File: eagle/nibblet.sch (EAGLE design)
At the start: 35 parts, among them IC1 MEGA8-AI

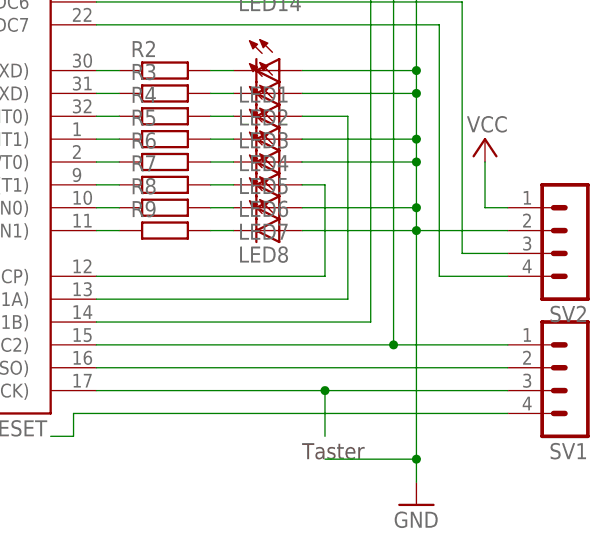
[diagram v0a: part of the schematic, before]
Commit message: consistent led order
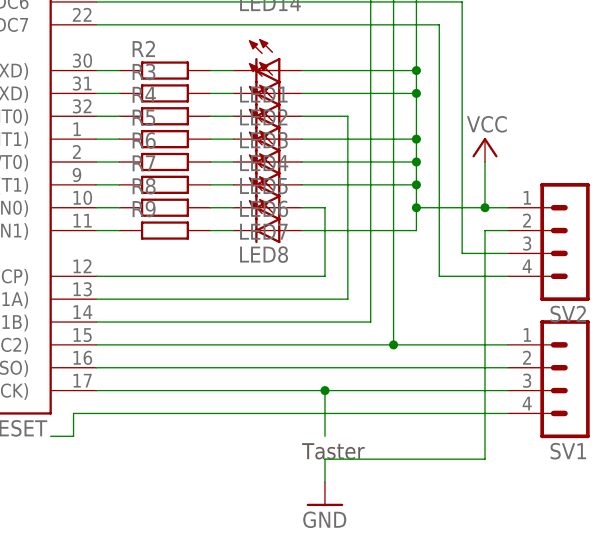
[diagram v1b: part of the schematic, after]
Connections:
- net GND: no longer LED1.A, LED11.A, LED12.A, LED13.A, LED2.A, LED4.A, LED5.A, LED7.A, LED8.A, LED9.A
- net N$23: now also LED7.A; no longer LED6.A
- net VCC: now also LED1.A, LED11.A, LED12.A, LED13.A, LED2.A, LED4.A, LED5.A, LED6.A, LED8.A, LED9.A
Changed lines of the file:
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@@
 <instance part="C2" gate="G$1" x="15.24" y="88.9" rot="R180"/>
 <instance part="P+2" gate="VCC" x="10.16" y="63.5"/>
-<instance part="GND2" gate="1" x="106.68" y="25.4"/>
+<instance part="GND2" gate="1" x="96.52" y="25.4"/>
 <instance part="PAD1" gate="G$1" x="5.08" y="86.36"/>
 <instance part="SV1" gate="1" x="124.46" y="38.1" rot="R180"/>
@@
 <pinref part="P+3" gate="VCC" pin="VCC"/>
 <pinref part="SV2" gate="1" pin="1"/>
+<wire x1="106.68" y1="96.52" x2="106.68" y2="91.44" width="0.1524" layer="91"/>
+<wire x1="106.68" y1="91.44" x2="106.68" y2="88.9" width="0.1524" layer="91"/>
+<wire x1="106.68" y1="88.9" x2="106.68" y2="86.36" width="0.1524" layer="91"/>
+<wire x1="106.68" y1="86.36" x2="106.68" y2="73.66" width="0.1524" layer="91"/>
+<wire x1="106.68" y1="73.66" x2="106.68" y2="71.12" width="0.1524" layer="91"/>
+<wire x1="106.68" y1="71.12" x2="106.68" y2="66.04" width="0.1524" layer="91"/>
+<wire x1="106.68" y1="66.04" x2="106.68" y2="63.5" width="0.1524" layer="91"/>
+<wire x1="106.68" y1="63.5" x2="106.68" y2="60.96" width="0.1524" layer="91"/>
+<wire x1="106.68" y1="60.96" x2="106.68" y2="58.42" width="0.1524" layer="91"/>
+<pinref part="LED9" gate="G$1" pin="A"/>
+<wire x1="106.68" y1="58.42" x2="106.68" y2="55.88" width="0.1524" layer="91"/>
+<wire x1="93.98" y1="96.52" x2="106.68" y2="96.52" width="0.1524" layer="91"/>
+<pinref part="LED11" gate="G$1" pin="A"/>
+<wire x1="93.98" y1="91.44" x2="106.68" y2="91.44" width="0.1524" layer="91"/>
+<junction x="106.68" y="91.44"/>
+<pinref part="LED12" gate="G$1" pin="A"/>
+<wire x1="93.98" y1="88.9" x2="106.68" y2="88.9" width="0.1524" layer="91"/>
+<junction x="106.68" y="88.9"/>
+<pinref part="LED13" gate="G$1" pin="A"/>
+<wire x1="93.98" y1="86.36" x2="106.68" y2="86.36" width="0.1524" layer="91"/>
+<junction x="106.68" y="86.36"/>
+<pinref part="LED1" gate="G$1" pin="A"/>
+<wire x1="93.98" y1="73.66" x2="106.68" y2="73.66" width="0.1524" layer="91"/>
+<junction x="106.68" y="73.66"/>
+<pinref part="LED2" gate="G$1" pin="A"/>
+<wire x1="93.98" y1="71.12" x2="106.68" y2="71.12" width="0.1524" layer="91"/>
+<junction x="106.68" y="71.12"/>
+<pinref part="LED4" gate="G$1" pin="A"/>
+<wire x1="93.98" y1="66.04" x2="106.68" y2="66.04" width="0.1524" layer="91"/>
+<junction x="106.68" y="66.04"/>
+<pinref part="LED5" gate="G$1" pin="A"/>
+<wire x1="93.98" y1="63.5" x2="106.68" y2="63.5" width="0.1524" layer="91"/>
+<junction x="106.68" y="63.5"/>
+<pinref part="LED8" gate="G$1" pin="A"/>
+<wire x1="93.98" y1="55.88" x2="106.68" y2="55.88" width="0.1524" layer="91"/>
+<pinref part="LED6" gate="G$1" pin="A"/>
+<wire x1="93.98" y1="60.96" x2="106.68" y2="60.96" width="0.1524" layer="91"/>
+<junction x="106.68" y="60.96"/>
+<wire x1="114.3" y1="58.42" x2="106.68" y2="58.42" width="0.1524" layer="91"/>
+<junction x="114.3" y="58.42"/>
+<junction x="106.68" y="58.42"/>
 </segment>
 </net>
@@
 </segment>
 <segment>
-<wire x1="106.68" y1="96.52" x2="106.68" y2="91.44" width="0.1524" layer="91"/>
-<wire x1="106.68" y1="91.44" x2="106.68" y2="88.9" width="0.1524" layer="91"/>
-<wire x1="106.68" y1="88.9" x2="106.68" y2="86.36" width="0.1524" layer="91"/>
-<wire x1="106.68" y1="86.36" x2="106.68" y2="73.66" width="0.1524" layer="91"/>
-<wire x1="106.68" y1="73.66" x2="106.68" y2="71.12" width="0.1524" layer="91"/>
-<wire x1="106.68" y1="71.12" x2="106.68" y2="66.04" width="0.1524" layer="91"/>
-<wire x1="106.68" y1="66.04" x2="106.68" y2="63.5" width="0.1524" layer="91"/>
-<wire x1="106.68" y1="63.5" x2="106.68" y2="58.42" width="0.1524" layer="91"/>
-<wire x1="106.68" y1="58.42" x2="106.68" y2="55.88" width="0.1524" layer="91"/>
-<wire x1="106.68" y1="55.88" x2="106.68" y2="30.48" width="0.1524" layer="91"/>
-<wire x1="106.68" y1="30.48" x2="106.68" y2="27.94" width="0.1524" layer="91"/>
-<wire x1="106.68" y1="55.88" x2="116.84" y2="55.88" width="0.1524" layer="91"/>
-<wire x1="96.52" y1="30.48" x2="106.68" y2="30.48" width="0.1524" layer="91"/>
-<junction x="106.68" y="55.88"/>
-<junction x="106.68" y="30.48"/>
 <pinref part="GND2" gate="1" pin="GND"/>
+<wire x1="96.52" y1="30.48" x2="96.52" y2="27.94" width="0.1524" layer="91"/>
 <pinref part="SV2" gate="1" pin="2"/>
-<pinref part="LED9" gate="G$1" pin="A"/>
-<wire x1="93.98" y1="96.52" x2="106.68" y2="96.52" width="0.1524" layer="91"/>
-<pinref part="LED11" gate="G$1" pin="A"/>
-<wire x1="93.98" y1="91.44" x2="106.68" y2="91.44" width="0.1524" layer="91"/>
-<junction x="106.68" y="91.44"/>
-<pinref part="LED12" gate="G$1" pin="A"/>
-<wire x1="93.98" y1="88.9" x2="106.68" y2="88.9" width="0.1524" layer="91"/>
-<junction x="106.68" y="88.9"/>
-<pinref part="LED13" gate="G$1" pin="A"/>
-<wire x1="93.98" y1="86.36" x2="106.68" y2="86.36" width="0.1524" layer="91"/>
-<junction x="106.68" y="86.36"/>
-<pinref part="LED1" gate="G$1" pin="A"/>
-<wire x1="93.98" y1="73.66" x2="106.68" y2="73.66" width="0.1524" layer="91"/>
-<junction x="106.68" y="73.66"/>
-<pinref part="LED2" gate="G$1" pin="A"/>
-<wire x1="93.98" y1="71.12" x2="106.68" y2="71.12" width="0.1524" layer="91"/>
-<junction x="106.68" y="71.12"/>
-<pinref part="LED4" gate="G$1" pin="A"/>
-<wire x1="93.98" y1="66.04" x2="106.68" y2="66.04" width="0.1524" layer="91"/>
-<junction x="106.68" y="66.04"/>
-<pinref part="LED5" gate="G$1" pin="A"/>
-<wire x1="93.98" y1="63.5" x2="106.68" y2="63.5" width="0.1524" layer="91"/>
-<junction x="106.68" y="63.5"/>
-<pinref part="LED7" gate="G$1" pin="A"/>
-<wire x1="93.98" y1="58.42" x2="106.68" y2="58.42" width="0.1524" layer="91"/>
-<junction x="106.68" y="58.42"/>
-<pinref part="LED8" gate="G$1" pin="A"/>
-<wire x1="93.98" y1="55.88" x2="106.68" y2="55.88" width="0.1524" layer="91"/>
+<wire x1="116.84" y1="55.88" x2="114.3" y2="55.88" width="0.1524" layer="91"/>
+<wire x1="114.3" y1="55.88" x2="114.3" y2="30.48" width="0.1524" layer="91"/>
+<wire x1="114.3" y1="30.48" x2="96.52" y2="30.48" width="0.1524" layer="91"/>
 </segment>
 </net>
@@
 <net name="N$23" class="0">
 <segment>
-<wire x1="96.52" y1="60.96" x2="96.52" y2="50.8" width="0.1524" layer="91"/>
 <wire x1="96.52" y1="50.8" x2="71.12" y2="50.8" width="0.1524" layer="91"/>
 <pinref part="IC1" gate="G$1" pin="PB0(ICP)"/>
-<pinref part="LED6" gate="G$1" pin="A"/>
-<wire x1="93.98" y1="60.96" x2="96.52" y2="60.96" width="0.1524" layer="91"/>
+<pinref part="LED7" gate="G$1" pin="A"/>
+<wire x1="93.98" y1="58.42" x2="96.52" y2="58.42" width="0.1524" layer="91"/>
+<wire x1="96.52" y1="58.42" x2="96.52" y2="50.8" width="0.1524" layer="91"/>
 </segment>
 </net>

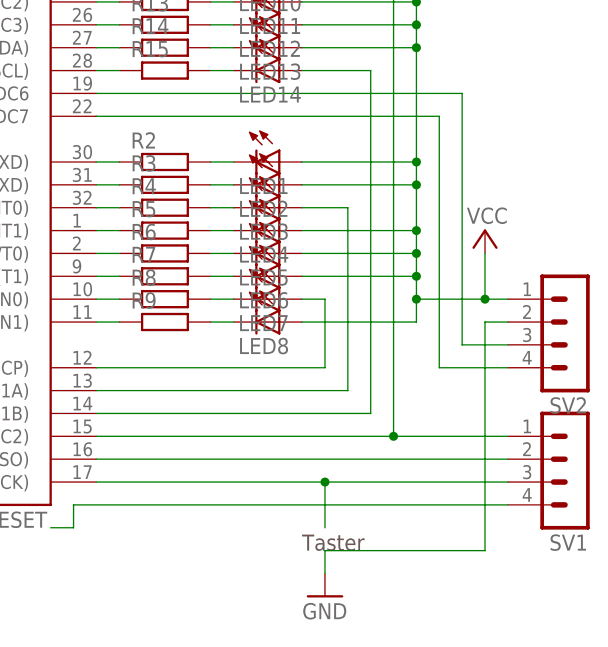
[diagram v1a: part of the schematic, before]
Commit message: led position really consistent
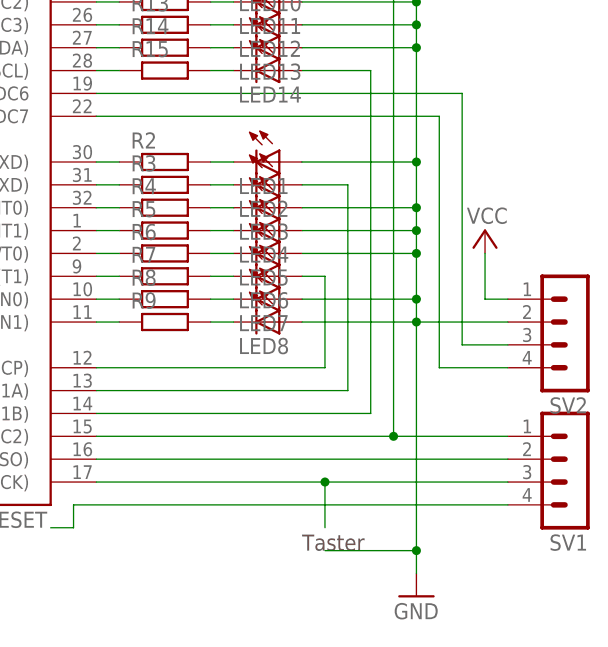
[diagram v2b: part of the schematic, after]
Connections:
- net GND: now also LED1.A, LED11.A, LED12.A, LED13.A, LED3.A, LED4.A, LED5.A, LED7.A, LED8.A, LED9.A
- net N$22: now also LED2.A; no longer LED3.A
- net N$23: now also LED6.A; no longer LED7.A
- net VCC: no longer LED1.A, LED11.A, LED12.A, LED13.A, LED2.A, LED4.A, LED5.A, LED6.A, LED8.A, LED9.A
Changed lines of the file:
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@@
 <instance part="C2" gate="G$1" x="15.24" y="88.9" rot="R180"/>
 <instance part="P+2" gate="VCC" x="10.16" y="63.5"/>
-<instance part="GND2" gate="1" x="96.52" y="25.4"/>
+<instance part="GND2" gate="1" x="106.68" y="25.4"/>
 <instance part="PAD1" gate="G$1" x="5.08" y="86.36"/>
 <instance part="SV1" gate="1" x="124.46" y="38.1" rot="R180"/>
@@
 <pinref part="P+3" gate="VCC" pin="VCC"/>
 <pinref part="SV2" gate="1" pin="1"/>
-<wire x1="106.68" y1="96.52" x2="106.68" y2="91.44" width="0.1524" layer="91"/>
-<wire x1="106.68" y1="91.44" x2="106.68" y2="88.9" width="0.1524" layer="91"/>
-<wire x1="106.68" y1="88.9" x2="106.68" y2="86.36" width="0.1524" layer="91"/>
-<wire x1="106.68" y1="86.36" x2="106.68" y2="73.66" width="0.1524" layer="91"/>
-<wire x1="106.68" y1="73.66" x2="106.68" y2="71.12" width="0.1524" layer="91"/>
-<wire x1="106.68" y1="71.12" x2="106.68" y2="66.04" width="0.1524" layer="91"/>
-<wire x1="106.68" y1="66.04" x2="106.68" y2="63.5" width="0.1524" layer="91"/>
-<wire x1="106.68" y1="63.5" x2="106.68" y2="60.96" width="0.1524" layer="91"/>
-<wire x1="106.68" y1="60.96" x2="106.68" y2="58.42" width="0.1524" layer="91"/>
-<pinref part="LED9" gate="G$1" pin="A"/>
-<wire x1="106.68" y1="58.42" x2="106.68" y2="55.88" width="0.1524" layer="91"/>
-<wire x1="93.98" y1="96.52" x2="106.68" y2="96.52" width="0.1524" layer="91"/>
-<pinref part="LED11" gate="G$1" pin="A"/>
-<wire x1="93.98" y1="91.44" x2="106.68" y2="91.44" width="0.1524" layer="91"/>
-<junction x="106.68" y="91.44"/>
-<pinref part="LED12" gate="G$1" pin="A"/>
-<wire x1="93.98" y1="88.9" x2="106.68" y2="88.9" width="0.1524" layer="91"/>
-<junction x="106.68" y="88.9"/>
-<pinref part="LED13" gate="G$1" pin="A"/>
-<wire x1="93.98" y1="86.36" x2="106.68" y2="86.36" width="0.1524" layer="91"/>
-<junction x="106.68" y="86.36"/>
-<pinref part="LED1" gate="G$1" pin="A"/>
-<wire x1="93.98" y1="73.66" x2="106.68" y2="73.66" width="0.1524" layer="91"/>
-<junction x="106.68" y="73.66"/>
-<pinref part="LED2" gate="G$1" pin="A"/>
-<wire x1="93.98" y1="71.12" x2="106.68" y2="71.12" width="0.1524" layer="91"/>
-<junction x="106.68" y="71.12"/>
-<pinref part="LED4" gate="G$1" pin="A"/>
-<wire x1="93.98" y1="66.04" x2="106.68" y2="66.04" width="0.1524" layer="91"/>
-<junction x="106.68" y="66.04"/>
-<pinref part="LED5" gate="G$1" pin="A"/>
-<wire x1="93.98" y1="63.5" x2="106.68" y2="63.5" width="0.1524" layer="91"/>
-<junction x="106.68" y="63.5"/>
-<pinref part="LED8" gate="G$1" pin="A"/>
-<wire x1="93.98" y1="55.88" x2="106.68" y2="55.88" width="0.1524" layer="91"/>
-<pinref part="LED6" gate="G$1" pin="A"/>
-<wire x1="93.98" y1="60.96" x2="106.68" y2="60.96" width="0.1524" layer="91"/>
-<junction x="106.68" y="60.96"/>
-<wire x1="114.3" y1="58.42" x2="106.68" y2="58.42" width="0.1524" layer="91"/>
-<junction x="114.3" y="58.42"/>
-<junction x="106.68" y="58.42"/>
 </segment>
 </net>
@@
 </segment>
 <segment>
+<wire x1="106.68" y1="96.52" x2="106.68" y2="91.44" width="0.1524" layer="91"/>
+<wire x1="106.68" y1="91.44" x2="106.68" y2="88.9" width="0.1524" layer="91"/>
+<wire x1="106.68" y1="88.9" x2="106.68" y2="86.36" width="0.1524" layer="91"/>
+<wire x1="106.68" y1="86.36" x2="106.68" y2="73.66" width="0.1524" layer="91"/>
+<wire x1="106.68" y1="73.66" x2="106.68" y2="68.58" width="0.1524" layer="91"/>
+<wire x1="106.68" y1="68.58" x2="106.68" y2="66.04" width="0.1524" layer="91"/>
+<wire x1="106.68" y1="66.04" x2="106.68" y2="63.5" width="0.1524" layer="91"/>
+<wire x1="106.68" y1="63.5" x2="106.68" y2="58.42" width="0.1524" layer="91"/>
+<wire x1="106.68" y1="58.42" x2="106.68" y2="55.88" width="0.1524" layer="91"/>
+<wire x1="106.68" y1="55.88" x2="106.68" y2="30.48" width="0.1524" layer="91"/>
+<wire x1="106.68" y1="30.48" x2="106.68" y2="27.94" width="0.1524" layer="91"/>
+<wire x1="106.68" y1="55.88" x2="116.84" y2="55.88" width="0.1524" layer="91"/>
+<wire x1="96.52" y1="30.48" x2="106.68" y2="30.48" width="0.1524" layer="91"/>
+<junction x="106.68" y="55.88"/>
+<junction x="106.68" y="30.48"/>
 <pinref part="GND2" gate="1" pin="GND"/>
-<wire x1="96.52" y1="30.48" x2="96.52" y2="27.94" width="0.1524" layer="91"/>
 <pinref part="SV2" gate="1" pin="2"/>
-<wire x1="116.84" y1="55.88" x2="114.3" y2="55.88" width="0.1524" layer="91"/>
-<wire x1="114.3" y1="55.88" x2="114.3" y2="30.48" width="0.1524" layer="91"/>
-<wire x1="114.3" y1="30.48" x2="96.52" y2="30.48" width="0.1524" layer="91"/>
+<pinref part="LED9" gate="G$1" pin="A"/>
+<wire x1="93.98" y1="96.52" x2="106.68" y2="96.52" width="0.1524" layer="91"/>
+<pinref part="LED11" gate="G$1" pin="A"/>
+<wire x1="93.98" y1="91.44" x2="106.68" y2="91.44" width="0.1524" layer="91"/>
+<junction x="106.68" y="91.44"/>
+<pinref part="LED12" gate="G$1" pin="A"/>
+<wire x1="93.98" y1="88.9" x2="106.68" y2="88.9" width="0.1524" layer="91"/>
+<junction x="106.68" y="88.9"/>
+<pinref part="LED13" gate="G$1" pin="A"/>
+<wire x1="93.98" y1="86.36" x2="106.68" y2="86.36" width="0.1524" layer="91"/>
+<junction x="106.68" y="86.36"/>
+<pinref part="LED1" gate="G$1" pin="A"/>
+<wire x1="93.98" y1="73.66" x2="106.68" y2="73.66" width="0.1524" layer="91"/>
+<junction x="106.68" y="73.66"/>
+<pinref part="LED4" gate="G$1" pin="A"/>
+<wire x1="93.98" y1="66.04" x2="106.68" y2="66.04" width="0.1524" layer="91"/>
+<junction x="106.68" y="66.04"/>
+<pinref part="LED5" gate="G$1" pin="A"/>
+<wire x1="93.98" y1="63.5" x2="106.68" y2="63.5" width="0.1524" layer="91"/>
+<junction x="106.68" y="63.5"/>
+<pinref part="LED7" gate="G$1" pin="A"/>
+<wire x1="93.98" y1="58.42" x2="106.68" y2="58.42" width="0.1524" layer="91"/>
+<junction x="106.68" y="58.42"/>
+<pinref part="LED8" gate="G$1" pin="A"/>
+<wire x1="93.98" y1="55.88" x2="106.68" y2="55.88" width="0.1524" layer="91"/>
+<pinref part="LED3" gate="G$1" pin="A"/>
+<wire x1="93.98" y1="68.58" x2="106.68" y2="68.58" width="0.1524" layer="91"/>
+<junction x="106.68" y="68.58"/>
 </segment>
 </net>
@@
 <net name="N$22" class="0">
 <segment>
-<wire x1="99.06" y1="68.58" x2="99.06" y2="48.26" width="0.1524" layer="91"/>
 <wire x1="99.06" y1="48.26" x2="71.12" y2="48.26" width="0.1524" layer="91"/>
 <pinref part="IC1" gate="G$1" pin="PB1(OC1A)"/>
-<pinref part="LED3" gate="G$1" pin="A"/>
-<wire x1="93.98" y1="68.58" x2="99.06" y2="68.58" width="0.1524" layer="91"/>
+<pinref part="LED2" gate="G$1" pin="A"/>
+<wire x1="93.98" y1="71.12" x2="99.06" y2="71.12" width="0.1524" layer="91"/>
+<wire x1="99.06" y1="71.12" x2="99.06" y2="48.26" width="0.1524" layer="91"/>
 </segment>
 </net>
 <net name="N$23" class="0">
 <segment>
+<wire x1="96.52" y1="60.96" x2="96.52" y2="50.8" width="0.1524" layer="91"/>
 <wire x1="96.52" y1="50.8" x2="71.12" y2="50.8" width="0.1524" layer="91"/>
 <pinref part="IC1" gate="G$1" pin="PB0(ICP)"/>
-<pinref part="LED7" gate="G$1" pin="A"/>
-<wire x1="93.98" y1="58.42" x2="96.52" y2="58.42" width="0.1524" layer="91"/>
-<wire x1="96.52" y1="58.42" x2="96.52" y2="50.8" width="0.1524" layer="91"/>
+<pinref part="LED6" gate="G$1" pin="A"/>
+<wire x1="93.98" y1="60.96" x2="96.52" y2="60.96" width="0.1524" layer="91"/>
 </segment>
 </net>

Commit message: pad for battery. GND on the PCB??
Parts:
- added PAD2, PAD3: WIREPADSMD1,27-254, wirepad:WIREPADSMD1,27-254
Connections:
- net GND: now also PAD1.P, PAD2.P, PAD3.P
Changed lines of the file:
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@@
 <?xml version="1.0" encoding="utf-8"?>
 <!DOCTYPE eagle SYSTEM "eagle.dtd">
-<eagle version="6.4">
+<eagle version="6.5.0">
 <drawing>
 <settings>
@@
 <part name="R14" library="rcl" deviceset="R-EU_" device="R0805"/>
 <part name="R15" library="rcl" deviceset="R-EU_" device="R0805"/>
+<part name="PAD2" library="wirepad" deviceset="WIREPAD" device="SMD1,27-254"/>
+<part name="PAD3" library="wirepad" deviceset="WIREPAD" device="SMD1,27-254"/>
 </parts>
 <sheets>
@@
 <instance part="R14" gate="G$1" x="78.74" y="86.36"/>
 <instance part="R15" gate="G$1" x="78.74" y="83.82"/>
+<instance part="PAD2" gate="G$1" x="5.08" y="78.74"/>
+<instance part="PAD3" gate="G$1" x="5.08" y="93.98"/>
 </instances>
 <busses>
@@
 <pinref part="C1" gate="G$1" pin="1"/>
 <pinref part="C2" gate="G$1" pin="1"/>
-</segment>
-<segment>
+<pinref part="PAD1" gate="G$1" pin="P"/>
+<wire x1="15.24" y1="86.36" x2="10.16" y2="86.36" width="0.1524" layer="91"/>
+<pinref part="PAD3" gate="G$1" pin="P"/>
+<wire x1="10.16" y1="86.36" x2="7.62" y2="86.36" width="0.1524" layer="91"/>
+<wire x1="7.62" y1="93.98" x2="10.16" y2="93.98" width="0.1524" layer="91"/>
+<wire x1="10.16" y1="93.98" x2="10.16" y2="86.36" width="0.1524" layer="91"/>
+<junction x="10.16" y="86.36"/>
+<wire x1="10.16" y1="86.36" x2="10.16" y2="78.74" width="0.1524" layer="91"/>
+<pinref part="PAD2" gate="G$1" pin="P"/>
+<wire x1="10.16" y1="78.74" x2="7.62" y2="78.74" width="0.1524" layer="91"/>
+</segment>
+<segment>
